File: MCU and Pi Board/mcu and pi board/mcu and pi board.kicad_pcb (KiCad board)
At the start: 4 copper layers, 143.6 x 215.8 mm, 115 parts, among them IC1 CSD17578Q3A, IC2 CSD17578Q3A, J1 BM04B-GHS-TBT, J10 430450428, J11 Conn_01x04_Pin, J12 Conn_01x02_Pin, J13 Conn_01x03_Pin, J14 ET60T-D04-0-00-D04-X-R1-S, J15 Conn_01x28_Socket, J16 Conn_01x28_Socket, J17 Conn_01x02_Pin, J18 Conn_01x04_Pin, J19 Conn_01x03_Pin, J2 ET60S-D04-3-08-D04-X-R1-S, J20 Conn_01x04_Pin, J21 Conn_01x02_Pin, J22 Conn_01x03_Pin, J23 Conn_02x02_Pin, J24 IPBT-105-H1-T-D-GP, J25 Conn_02x09_Counter_Clockwise, J26 Conn_01x03_Pin, J27 DebugnBoot, J28 UART-PINS, J29 Conn_01x03_Pin, J3 PJ-002A, J30 PWM Connector, J31 ESC ADAPTER - BACKPLANE, J32 TB006-508-03BE, J33 TB006-508-03BE, J34 TB006-508-03BE, J4 Conn_01x04_Socket, J5 PJ-002A, J6 IPBT-105-H1-T-D-GP, J7 Conn_02x04_Counter_Clockwise, J8 Conn_01x02_Pin, J9 Conn_01x05, Q1 BSC010N04LS6ATMA1, Q2 BSC010N04LS6ATMA1, U1 LTC4370CMS_PBF, U2 LM3940IMPX-3.3/NOPB, U3 STM32F091CCT6, U4 RASPBERRY_PI_4B_4GB, U5 MC74HC157ADR2G, U6 MC74HC157ADR2G, U7 TPS40305DRCR

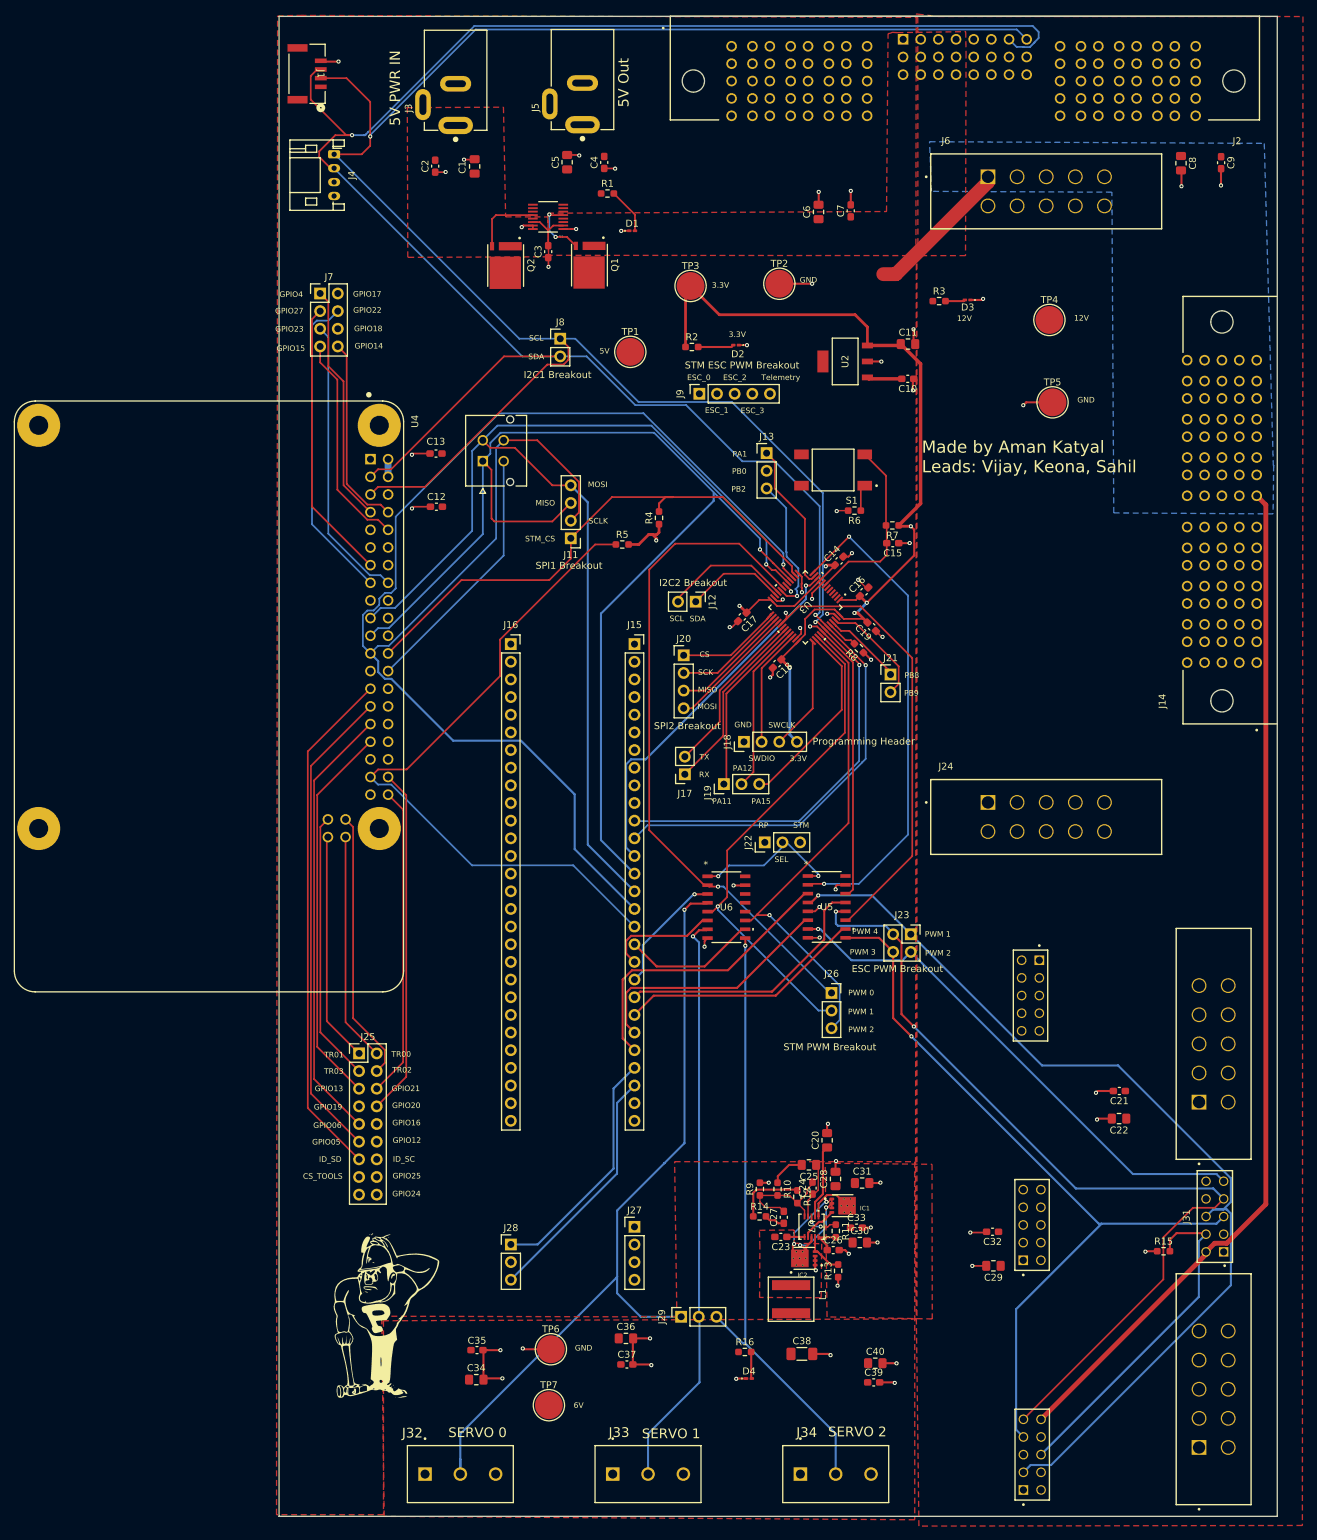
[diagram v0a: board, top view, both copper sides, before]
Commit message: added vias and some silkscreen art
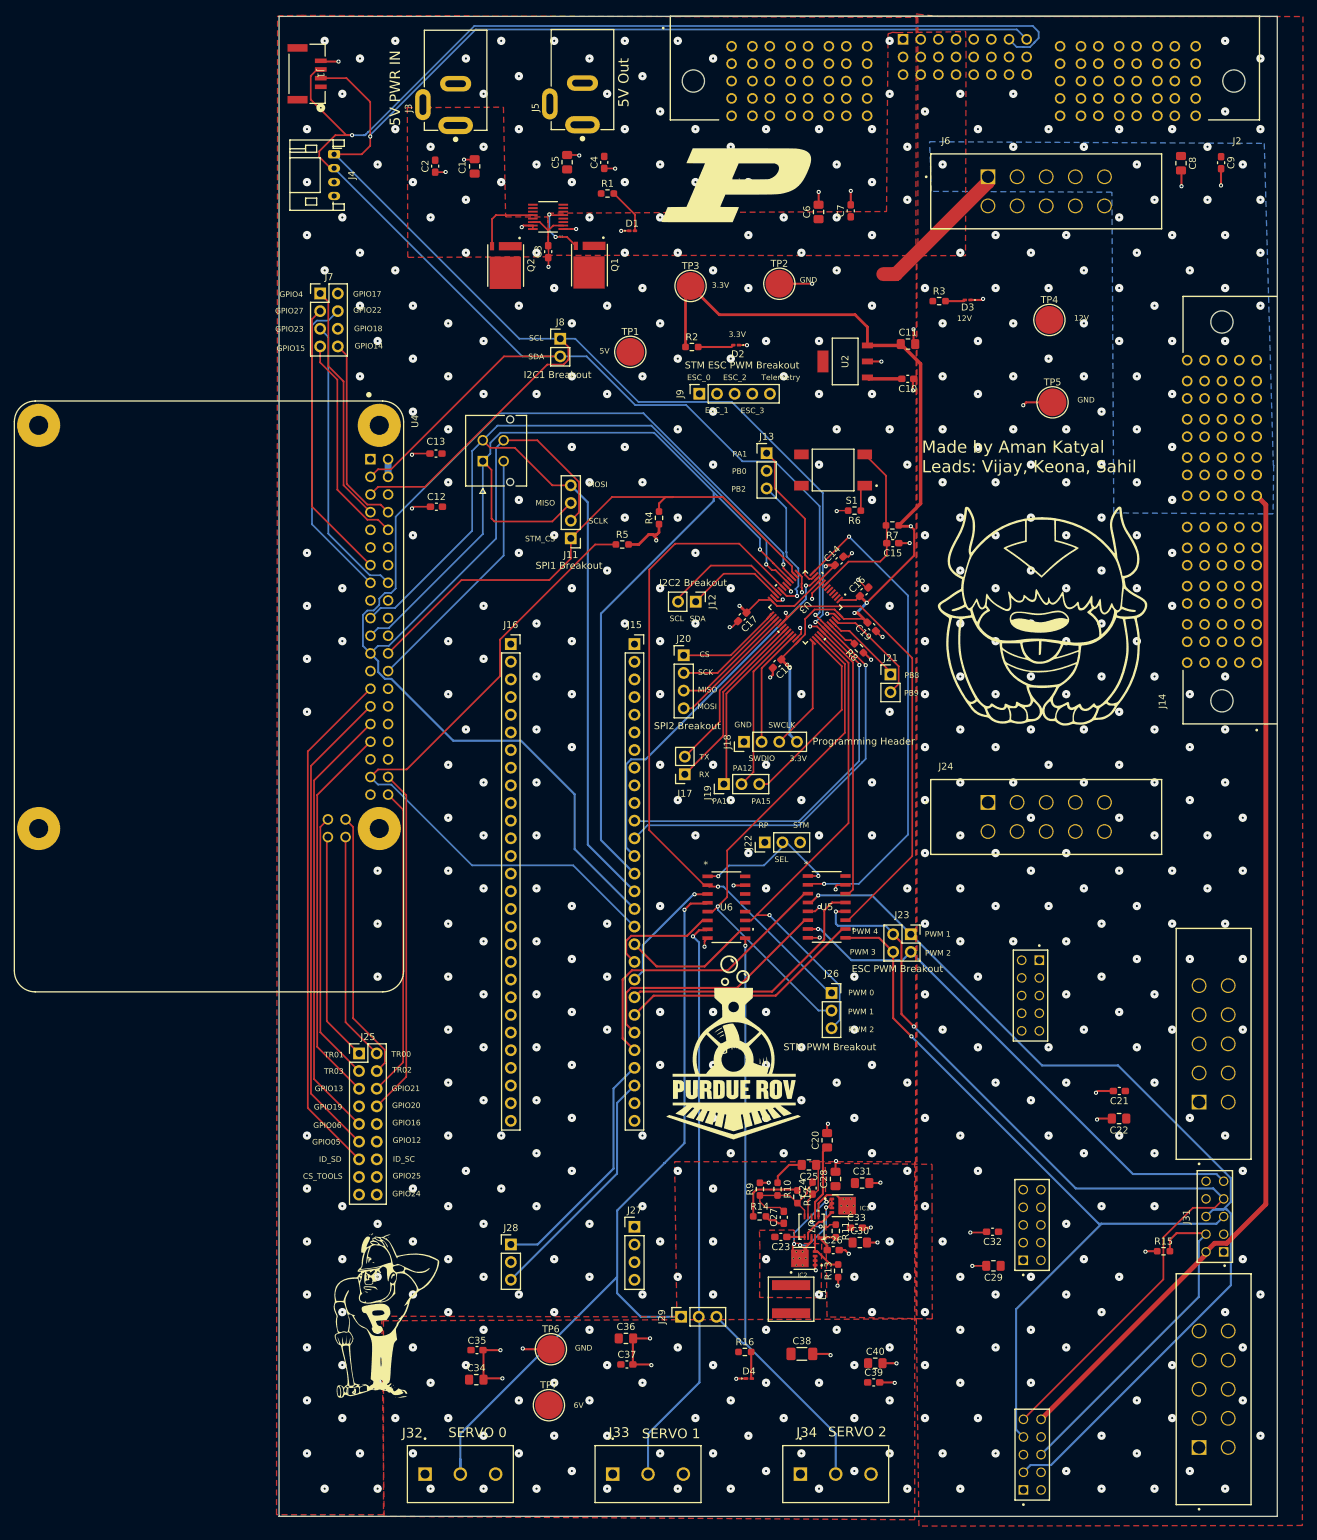
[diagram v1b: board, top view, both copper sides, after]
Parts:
- added G***: LOGO, LOGO, F.Cu at (224.4, 52.2)
- added G***: LOGO, LOGO, F.Cu at (268.8, 113.9)
- added G***: LOGO, LOGO, F.Cu at (224.4, 176.6)
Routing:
- net GND: vias 60 -> 584

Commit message: bom updated stuff
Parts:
- D1: footprint LED_SMD:LED_0201_0603Metric_Pad0.64x0.40mm_HandSolder -> LED_SMD:LED_0805_2012Metric_Pad1.15x1.40mm_HandSolder
- D2: value PURPLE_LED -> YELLOW_LED; footprint LED_SMD:LED_0201_0603Metric_Pad0.64x0.40mm_HandSolder -> LED_SMD:LED_0805_2012Metric_Pad1.15x1.40mm_HandSolder
- D3, D4: footprint LED_SMD:LED_0201_0603Metric_Pad0.64x0.40mm_HandSolder -> LED_SMD:LED_0603_1608Metric_Pad1.05x0.95mm_HandSolder
- R2: value 270 -> 100
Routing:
- net Net-(D2-A): track 5.16 -> 4.17 mm
- net Net-(D3-A): track 2.85 -> 2.15 mm
- net GND: track 126.2 -> 125.7 mm
